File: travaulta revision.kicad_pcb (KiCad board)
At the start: 4 copper layers, 209.7 x 76.4 mm, 106 parts, among them SW1 EC_SW, SW10 EC_SW, SW11 EC_SW, SW12 EC_SW, SW13 EC_SW, SW14 EC_SW, SW15 EC_SW, SW16 EC_SW, SW17 EC_SW, SW18 EC_SW, SW19 EC_SW, SW2 EC_SW, SW20 EC_SW, SW21 EC_SW, SW22 EC_SW, SW23 EC_SW, SW24 EC_SW, SW25 EC_SW, SW26 EC_SW, SW27 EC_SW, SW28 EC_SW, SW29 EC_SW, SW3 EC_SW, SW30 EC_SW, SW31 EC_SW, SW32 EC_SW, SW33 EC_SW, SW34 EC_SW, SW35 EC_SW, SW36 EC_SW, SW37 EC_SW, SW38 BOOT0, SW4 EC_SW, SW5 EC_SW, SW6 EC_SW, SW7 EC_SW, SW8 EC_SW, SW9 EC_SW, U1 STM32F401CBUx, U2 XC6206PxxxMR, U3 74HC4051, U4 74HC4051, U5 OPA350, Y1 8 MHz

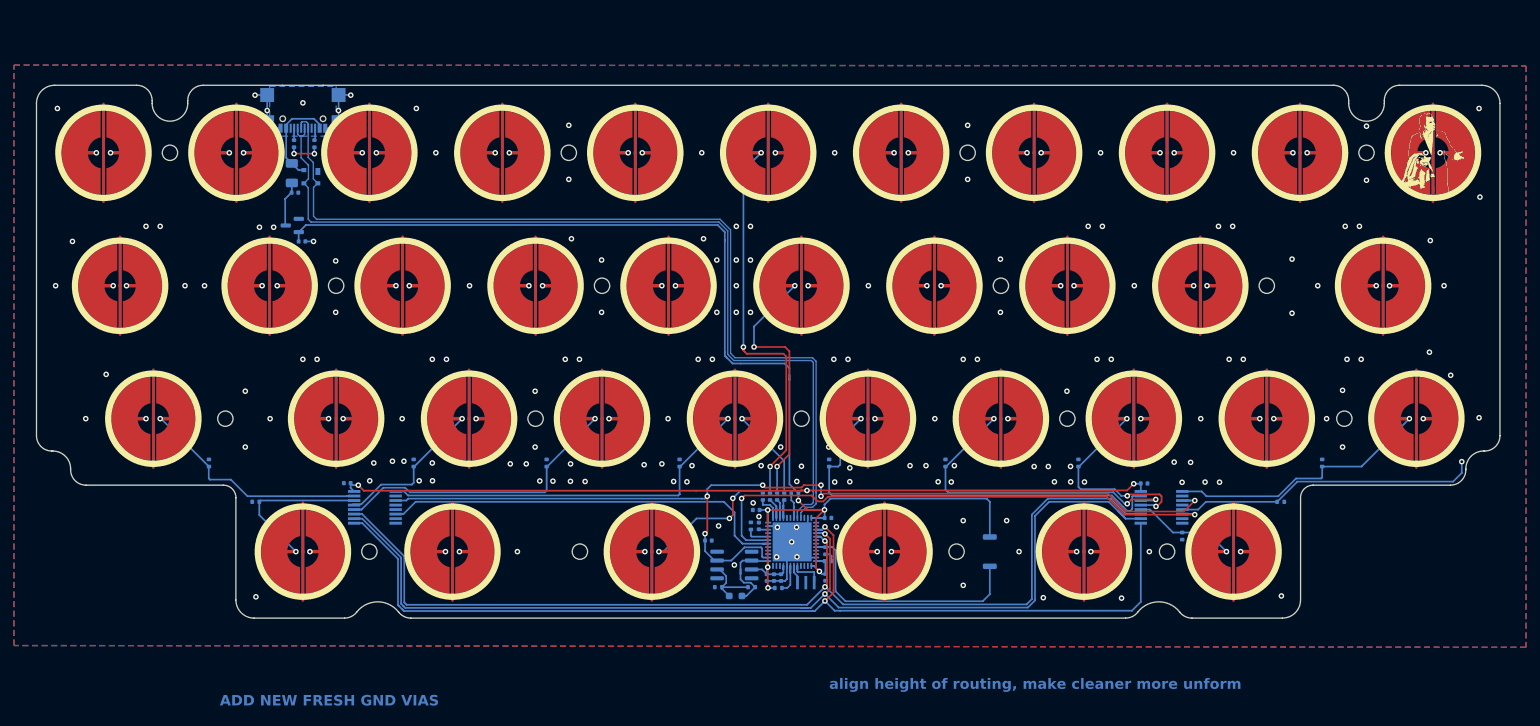
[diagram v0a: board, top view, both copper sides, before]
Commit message: GND via revision
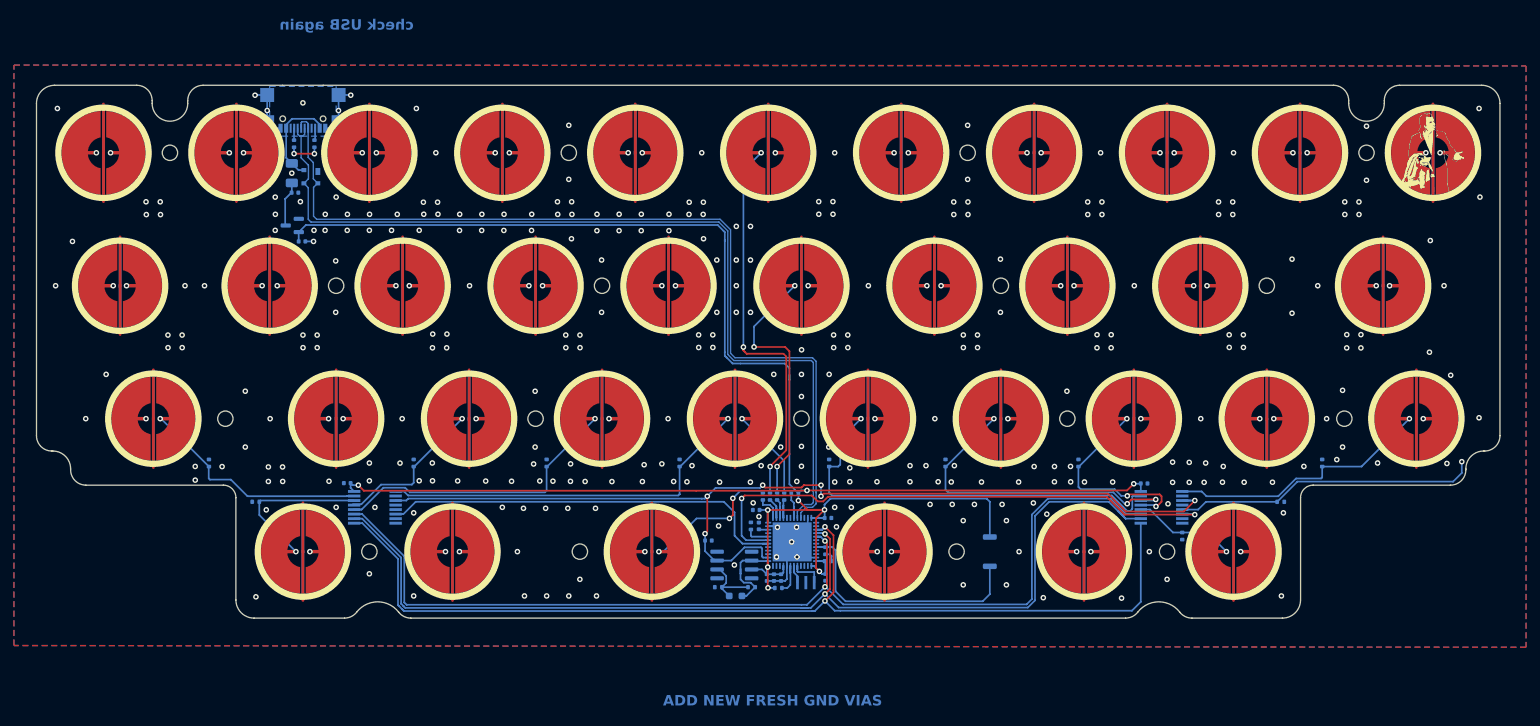
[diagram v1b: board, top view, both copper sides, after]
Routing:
- net APLEX_OUT_PIN_0: track 142.5 -> 141.9 mm
- net GND: vias 161 -> 302
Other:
- board text added: "check USB again"
- board text removed: "align height of routing, make cleaner more unform"

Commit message: revision routing further improved (edge problems addressed)
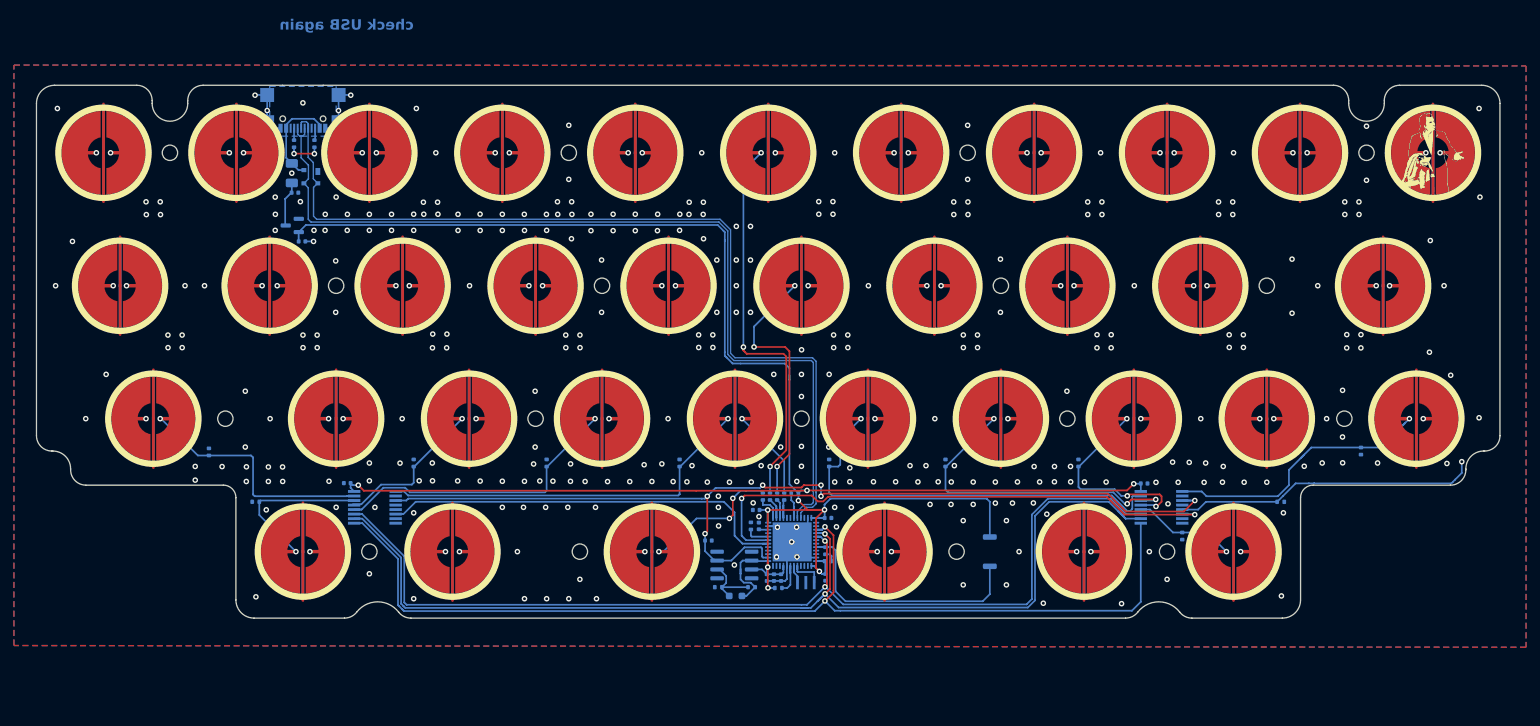
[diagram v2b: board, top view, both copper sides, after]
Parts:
- moved R16 5.81 mm to (234.2, 99.9), turned to -90 degrees
- moved R15 1.59 mm to (69.1, 100.0)
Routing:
- net ROW3: track 216.6 -> 222.5 mm
- net COL9: track 85.4 -> 91.0 mm
- net COL0: track 79.3 -> 81.4 mm
- net AMUX_SEL_1: track 152.1 -> 153.5 mm
- net GND: vias 302 -> 319
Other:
- board text removed: "ADD NEW FRESH GND VIAS"

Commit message: small tweaks
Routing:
- net GND: vias 319 -> 326
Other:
- board text removed: "check USB again"
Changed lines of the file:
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@@
   (gr_arc locked (start 249.184374 102.433999) (mid 249.931233 100.630857) (end 251.734375 99.884)
     (stroke (width 0.05) (type solid)) (layer "Edge.Cuts"))
-  (gr_text "check USB again" (at 98.425 39.6875) (layer "B.Cu")
-    (effects (font (size 1.5 1.5) (thickness 0.3) bold) (justify left bottom mirror))
-  )
   (gr_text "JLCJLCJLCJLC" (at 82.55 50.927) (layer "B.SilkS")
     (effects (font (size 1 1) (thickness 0.15)))
@@
   (via (at 207.9625 104.366597) (size 0.8) (drill 0.4) (layers "F.Cu" "B.Cu") (free) (net 1))
   (via (at 103.1875 83.125992) (size 0.8) (drill 0.4) (layers "F.Cu" "B.Cu") (free) (net 1))
-  (via (at 226.028066 102.066622) (size 0.8) (drill 0.4) (layers "F.Cu" "B.Cu") (net 1))
+  (via (at 226.028066 101.6) (size 0.8) (drill 0.4) (layers "F.Cu" "B.Cu") (net 1))
   (via (at 119.027099 64.169317) (size 0.8) (drill 0.4) (layers "F.Cu" "B.Cu") (free) (net 1))
   (via (at 77.43 51.094) (size 0.8) (drill 0.4) (layers "F.Cu" "B.Cu") (net 1))
@@
   (via (at 233.867827 64.186346) (size 0.8) (drill 0.4) (layers "F.Cu" "B.Cu") (free) (net 1))
   (via (at 158.602637 85.060062) (size 0.8) (drill 0.4) (layers "F.Cu" "B.Cu") (free) (net 1))
+  (via (at 144.68858 83.212362) (size 0.8) (drill 0.4) (layers "F.Cu" "B.Cu") (free) (net 1))
   (via (at 88.926415 65.964205) (size 0.8) (drill 0.4) (layers "F.Cu" "B.Cu") (free) (net 1))
   (via (at 142.113 110.617) (size 0.8) (drill 0.4) (layers "F.Cu" "B.Cu") (net 1))
@@
   (via (at 231.512224 97.872127) (size 0.8) (drill 0.4) (layers "F.Cu" "B.Cu") (net 1))
   (via (at 120.506079 107.95) (size 0.8) (drill 0.4) (layers "F.Cu" "B.Cu") (free) (net 1))
+  (via (at 144.716101 85.427602) (size 0.8) (drill 0.4) (layers "F.Cu" "B.Cu") (free) (net 1))
   (via (at 143.66875 104.344178) (size 0.8) (drill 0.4) (layers "F.Cu" "B.Cu") (free) (net 1))
   (via (at 92.075 104.154757) (size 0.8) (drill 0.4) (layers "F.Cu" "B.Cu") (free) (net 1))
@@
   (via (at 172.415783 107.530039) (size 0.8) (drill 0.4) (layers "F.Cu" "B.Cu") (free) (net 1))
   (via (at 130.175 68.309162) (size 0.8) (drill 0.4) (layers "F.Cu" "B.Cu") (free) (net 1))
-  (via (at 121.031 69.469) (size 0.8) (drill 0.4) (layers "F.Cu" "B.Cu") (free) (net 1))
   (via (at 160.911418 104.28102) (size 0.8) (drill 0.4) (layers "F.Cu" "B.Cu") (free) (net 1))
   (via (at 217.417014 104.354056) (size 0.8) (drill 0.4) (layers "F.Cu" "B.Cu") (free) (net 1))
@@
   (via (at 60.116776 66.008155) (size 0.8) (drill 0.4) (layers "F.Cu" "B.Cu") (free) (net 1))
   (via (at 98.425491 121.047612) (size 0.8) (drill 0.4) (layers "F.Cu" "B.Cu") (free) (net 1))
-  (via (at 139.954 69.469) (size 0.8) (drill 0.4) (layers "F.Cu" "B.Cu") (free) (net 1))
   (via (at 101.847881 64.231533) (size 0.8) (drill 0.4) (layers "F.Cu" "B.Cu") (free) (net 1))
   (via (at 104.728337 104.167899) (size 0.8) (drill 0.4) (layers "F.Cu" "B.Cu") (free) (net 1))
@@
   (via (at 68.453 76.2) (size 0.8) (drill 0.4) (layers "F.Cu" "B.Cu") (net 1))
   (via (at 201.676 76.2) (size 0.8) (drill 0.4) (layers "F.Cu" "B.Cu") (net 1))
+  (via (at 146.681488 64.206158) (size 0.8) (drill 0.4) (layers "F.Cu" "B.Cu") (free) (net 1))
   (via (at 192.024 91.313) (size 0.8) (drill 0.4) (layers "F.Cu" "B.Cu") (net 1))
   (via (at 231.835827 64.186346) (size 0.8) (drill 0.4) (layers "F.Cu" "B.Cu") (free) (net 1))
@@
   (via (at 77.602279 102.166606) (size 0.8) (drill 0.4) (layers "F.Cu" "B.Cu") (free) (net 1))
   (via (at 120.65 60.96) (size 0.8) (drill 0.4) (layers "F.Cu" "B.Cu") (free) (net 1))
+  (via (at 121.126329 68.333618) (size 0.8) (drill 0.4) (layers "F.Cu" "B.Cu") (free) (net 1))
   (via (at 220.6625 104.354056) (size 0.8) (drill 0.4) (layers "F.Cu" "B.Cu") (free) (net 1))
   (via (at 114.298033 104.219745) (size 0.8) (drill 0.4) (layers "F.Cu" "B.Cu") (free) (net 1))
@@
   (via (at 224.282 72.39) (size 0.8) (drill 0.4) (layers "F.Cu" "B.Cu") (net 1))
   (via (at 125.349 72.517) (size 0.8) (drill 0.4) (layers "F.Cu" "B.Cu") (net 1))
+  (via (at 148.586409 83.241559) (size 0.8) (drill 0.4) (layers "F.Cu" "B.Cu") (free) (net 1))
   (via (at 67.120529 104.050751) (size 0.8) (drill 0.4) (layers "F.Cu" "B.Cu") (free) (net 1))
   (via (at 195.003308 64.193631) (size 0.8) (drill 0.4) (layers "F.Cu" "B.Cu") (free) (net 1))
   (via (at 185.166 114.3) (size 0.8) (drill 0.4) (layers "F.Cu" "B.Cu") (net 1))
-  (via (at 157.89275 99.314) (size 0.8) (drill 0.4) (layers "F.Cu" "B.Cu") (free) (net 1))
+  (via (at 157.1625 99.314) (size 0.8) (drill 0.4) (layers "F.Cu" "B.Cu") (free) (net 1))
+  (via (at 101.911437 68.2625) (size 0.8) (drill 0.4) (layers "F.Cu" "B.Cu") (free) (net 1))
   (via (at 104.775 65.960003) (size 0.8) (drill 0.4) (layers "F.Cu" "B.Cu") (free) (net 1))
   (via (at 189.144827 108.929415) (size 0.8) (drill 0.4) (layers "F.Cu" "B.Cu") (free) (net 1))
@@
   (via (at 158.75 107.95) (size 0.8) (drill 0.4) (layers "F.Cu" "B.Cu") (free) (net 1))
   (via (at 74.295 99.314) (size 0.8) (drill 0.4) (layers "F.Cu" "B.Cu") (net 1))
+  (via (at 144.652281 64.206158) (size 0.8) (drill 0.4) (layers "F.Cu" "B.Cu") (free) (net 1))
   (via (at 144.653 80.01) (size 0.8) (drill 0.4) (layers "F.Cu" "B.Cu") (net 1))
   (via (at 251.079 95.123) (size 0.8) (drill 0.4) (layers "F.Cu" "B.Cu") (net 1))
@@
   (via (at 177.8 60.96) (size 0.8) (drill 0.4) (layers "F.Cu" "B.Cu") (free) (net 1))
   (via (at 215.79072 65.997413) (size 0.8) (drill 0.4) (layers "F.Cu" "B.Cu") (free) (net 1))
+  (via (at 139.953601 68.350091) (size 0.8) (drill 0.4) (layers "F.Cu" "B.Cu") (free) (net 1))
+  (via (at 228.6 98.425) (size 0.8) (drill 0.4) (layers "F.Cu" "B.Cu") (net 1))
   (via (at 153.346 115.062) (size 0.8) (drill 0.4) (layers "F.Cu" "B.Cu") (net 1))
   (via (at 87.653038 51.101306) (size 0.8) (drill 0.4) (layers "F.Cu" "B.Cu") (net 1))
@@
       )
     )
-  )
-  (zone (net 1) (net_name "GND") (layer "B.Cu") (hatch edge 0.508)
-    (priority 1)
-    (connect_pads (clearance 0))
-    (min_thickness 0.0254) (filled_areas_thickness no)
-    (fill yes (thermal_gap 0.508) (thermal_bridge_width 0.508) (island_removal_mode 1) (island_area_min 0))
-    (polygon
-      (pts
-        (xy 77.7875 47.625)
-        (xy 87.3125 47.625)
-        (xy 87.3125 54.76875)
-        (xy 77.7875 54.76875)
-      )
-    )
